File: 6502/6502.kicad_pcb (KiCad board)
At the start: 2 copper layers, 188.3 x 191.4 mm, 52 parts, among them J1 Conn_01x08, J10 Conn_02x20_Odd_Even, J11 Mini-DIN-6, J12 Conn_02x20_Odd_Even, J13 Jack-DC, J14 Conn_01x02, J2 Conn_01x08, J3 Conn_01x03, J4 Conn_02x20_Odd_Even, J5 Conn_01x08, J6 Conn_01x05, J7 Conn_02x20_Odd_Even, J8 Conn_01x02, J9 Conn_01x02, Q1 FQP47P06, SW1 SW_Push, SW2 SW_Push, U1 74LS08, U10 LM7805_TO220, U2 74LS154, U3 28C256, U4 ATF22V10C, U5 65C02S, U6 AS6C4008-55PCN, U7 6522, U8 6522, U9 NHD-0420H1Z, X1 ACO-4MHz

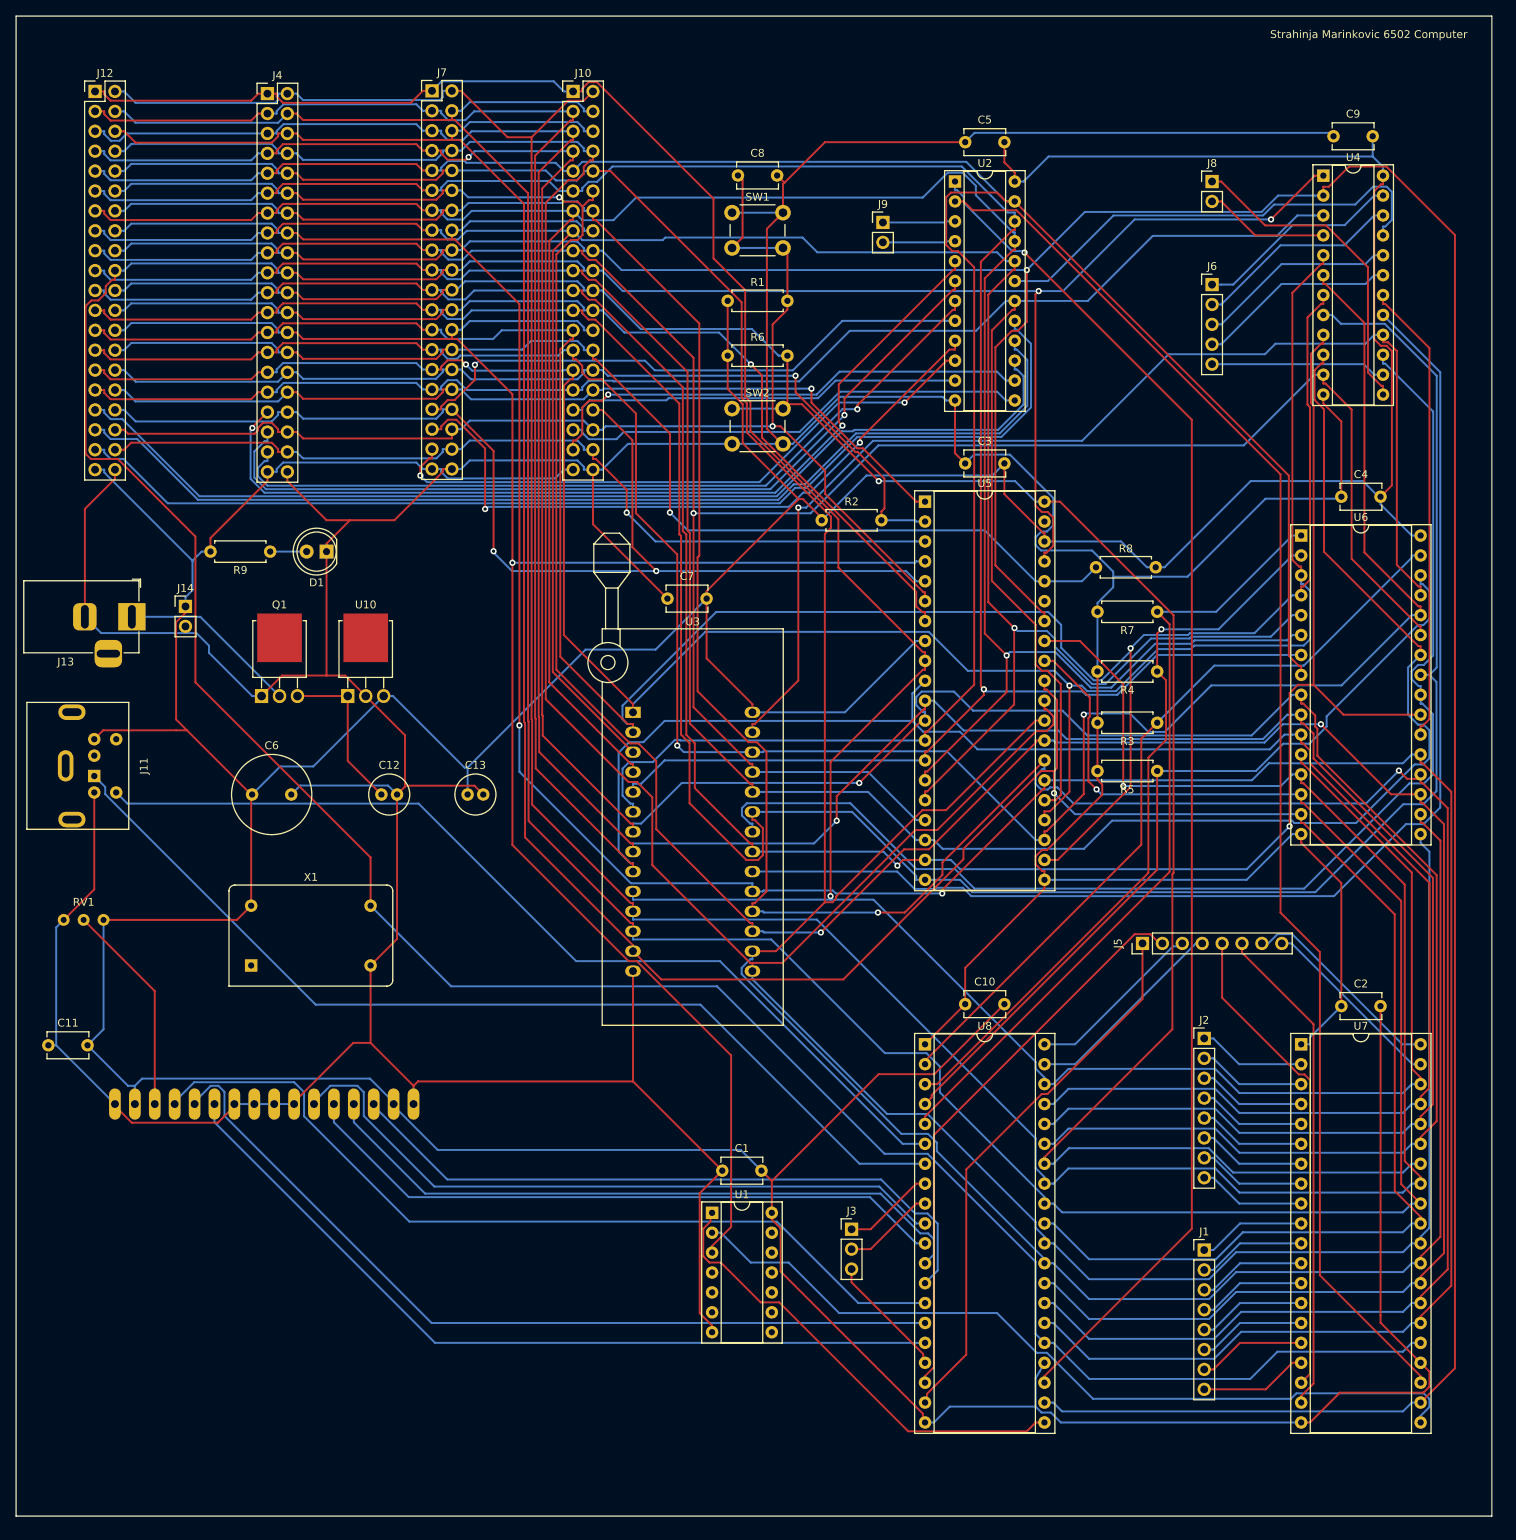
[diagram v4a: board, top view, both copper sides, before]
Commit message: added mount holes
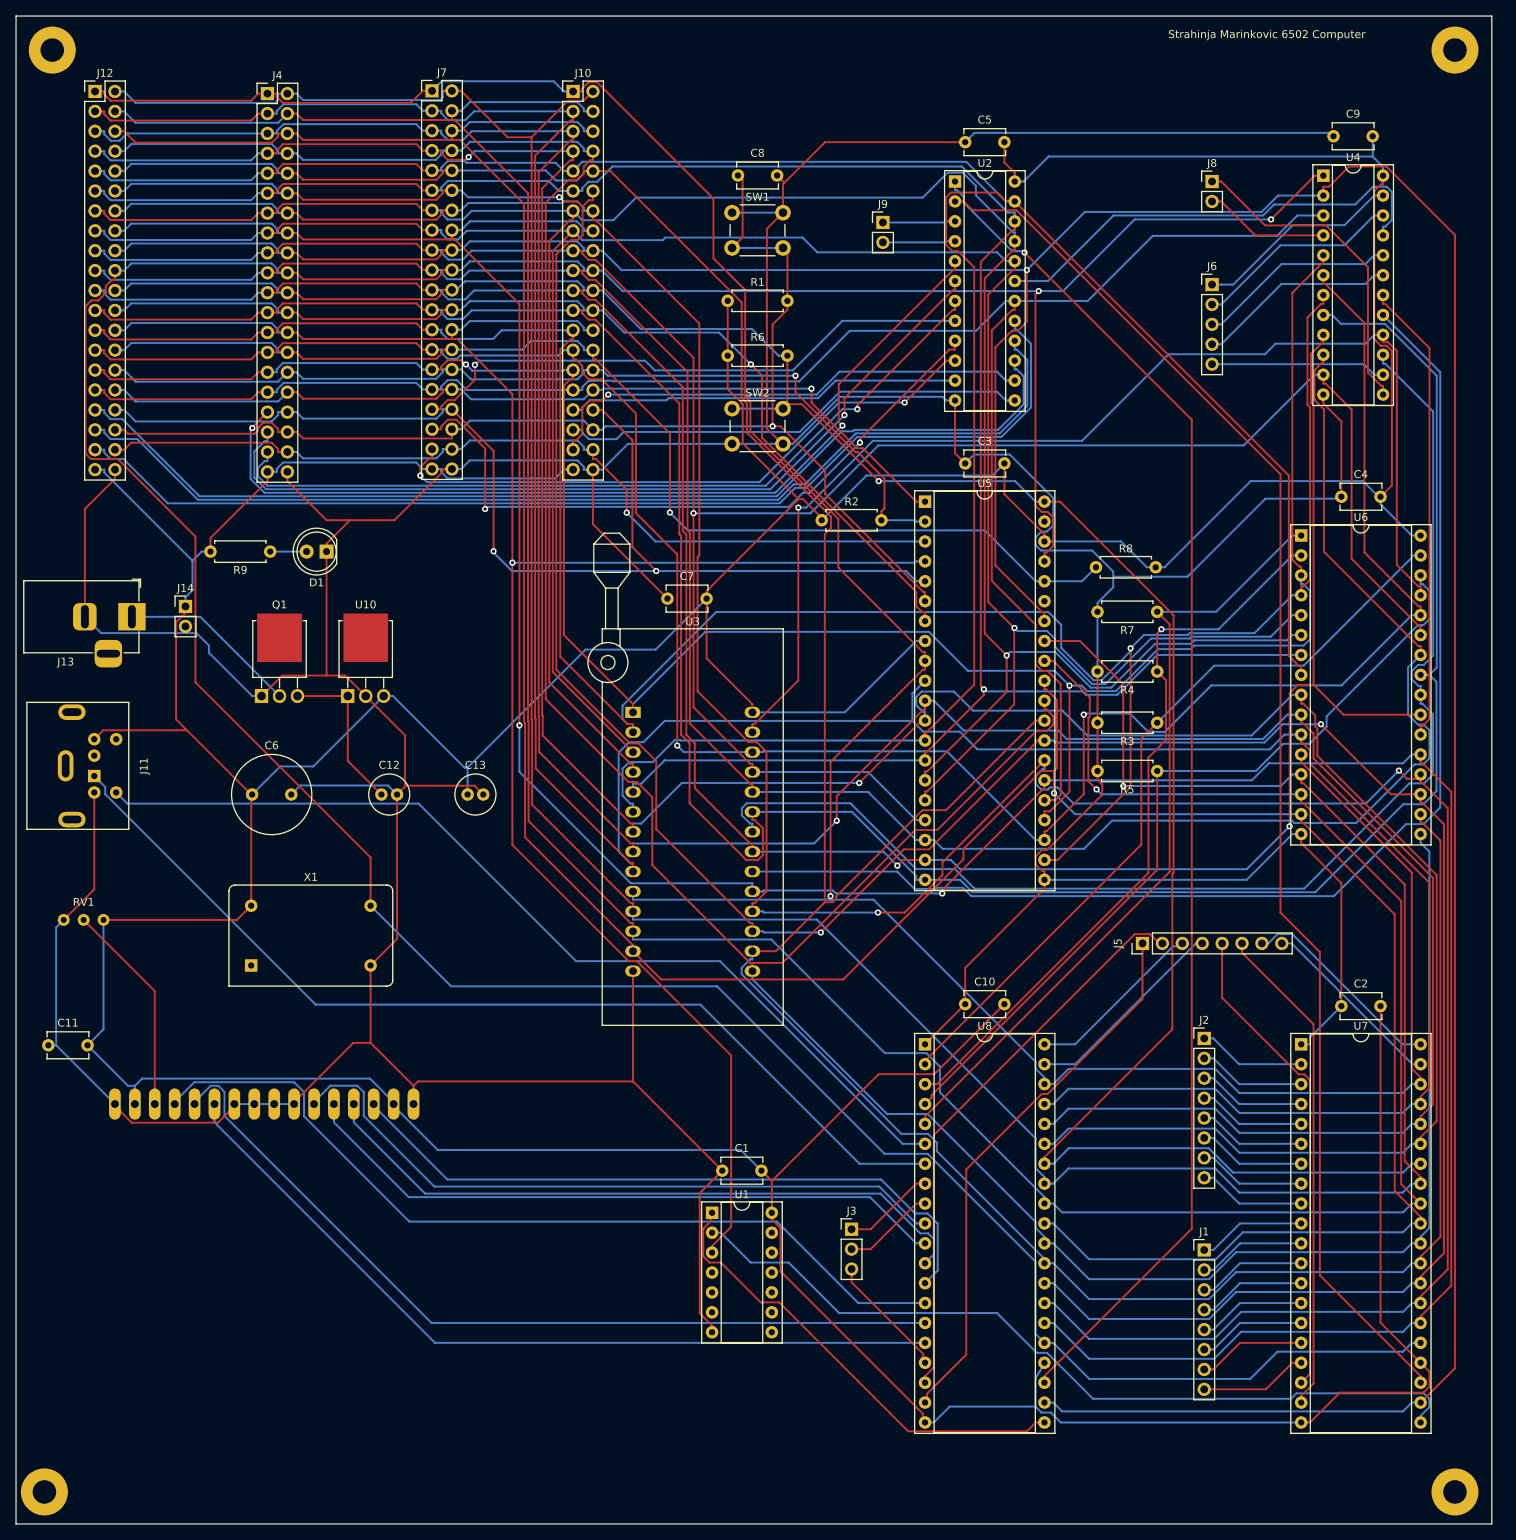
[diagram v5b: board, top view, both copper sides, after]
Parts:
- added REF**: MountingHole_3mm_Pad, MountingHole:MountingHole_3mm_Pad, F.Cu at (312.0, 259.0)
- added REF**: MountingHole_3mm_Pad, MountingHole:MountingHole_3mm_Pad, F.Cu at (133.0, 75.0)
- added REF**: MountingHole_3mm_Pad, MountingHole:MountingHole_3mm_Pad, F.Cu at (132.0, 259.0)
- added REF**: MountingHole_3mm_Pad, MountingHole:MountingHole_3mm_Pad, F.Cu at (312.0, 75.0)
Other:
- board size 188.3 x 191.4 mm -> 188.3 x 192.4 mm
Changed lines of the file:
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@@
     )
+  )
+  (footprint "MountingHole:MountingHole_3mm_Pad" (layer "F.Cu")
+    (at 312 259)
+    (descr "Mounting Hole 3mm")
+    (tags "mounting hole 3mm")
+    (attr exclude_from_pos_files exclude_from_bom)
+    (fp_text reference "REF**" (at 0 -5) (layer "F.SilkS") hide
+      (effects (font (size 1 1) (thickness 0.15)))
+    )
+    (fp_text value "MountingHole_3mm_Pad" (at 0 4) (layer "F.Fab")
+      (effects (font (size 1 1) (thickness 0.15)))
+    )
+    (fp_text user "${REFERENCE}" (at 0 0) (layer "F.Fab")
+      (effects (font (size 1 1) (thickness 0.15)))
+    )
+    (fp_circle (center 0 0) (end 3 0) (layer "Cmts.User") (width 0.15) (fill none))
+    (fp_circle (center 0 0) (end 3.25 0) (layer "F.CrtYd") (width 0.05) (fill none))
+    (pad "1" thru_hole circle (at 0 0) (size 6 6) (drill 3) (layers *.Cu *.Mask))
   )
   (footprint "Connector_PinHeader_2.54mm:PinHeader_2x20_P2.54mm_Vertical" (layer "F.Cu")
@@
       (rotate (xyz 0 0 0))
     )
+  )
+  (footprint "MountingHole:MountingHole_3mm_Pad" (layer "F.Cu")
+    (at 133 75)
+    (descr "Mounting Hole 3mm")
+    (tags "mounting hole 3mm")
+    (attr exclude_from_pos_files exclude_from_bom)
+    (fp_text reference "REF**" (at 0 -4) (layer "F.SilkS") hide
+      (effects (font (size 1 1) (thickness 0.15)))
+    )
+    (fp_text value "MountingHole_3mm_Pad" (at 0 4) (layer "F.Fab")
+      (effects (font (size 1 1) (thickness 0.15)))
+    )
+    (fp_text user "${REFERENCE}" (at 0 0) (layer "F.Fab")
+      (effects (font (size 1 1) (thickness 0.15)))
+    )
+    (fp_circle (center 0 0) (end 3 0) (layer "Cmts.User") (width 0.15) (fill none))
+    (fp_circle (center 0 0) (end 3.25 0) (layer "F.CrtYd") (width 0.05) (fill none))
+    (pad "1" thru_hole circle (at 0 0) (size 6 6) (drill 3) (layers *.Cu *.Mask))
   )
   (footprint "LED_THT:LED_D5.0mm_Clear" (layer "F.Cu")
@@
     )
   )
+  (footprint "MountingHole:MountingHole_3mm_Pad" (layer "F.Cu")
+    (at 132 259)
+    (descr "Mounting Hole 3mm")
+    (tags "mounting hole 3mm")
+    (attr exclude_from_pos_files exclude_from_bom)
+    (fp_text reference "REF**" (at 0 -4) (layer "F.SilkS") hide
+      (effects (font (size 1 1) (thickness 0.15)))
+    )
+    (fp_text value "MountingHole_3mm_Pad" (at 0 4) (layer "F.Fab")
+      (effects (font (size 1 1) (thickness 0.15)))
+    )
+    (fp_text user "${REFERENCE}" (at 0 0) (layer "F.Fab")
+      (effects (font (size 1 1) (thickness 0.15)))
+    )
+    (fp_circle (center 0 0) (end 3 0) (layer "Cmts.User") (width 0.15) (fill none))
+    (fp_circle (center 0 0) (end 3.25 0) (layer "F.CrtYd") (width 0.05) (fill none))
+    (pad "1" thru_hole circle (at 0 0) (size 6 6) (drill 3) (layers *.Cu *.Mask))
+  )
   (footprint "Resistor_THT:R_Axial_DIN0207_L6.3mm_D2.5mm_P7.62mm_Horizontal" (layer "F.Cu")
     (at 219.19 107)
@@
     )
   )
+  (footprint "MountingHole:MountingHole_3mm_Pad" (layer "F.Cu")
+    (at 312 75)
+    (descr "Mounting Hole 3mm")
+    (tags "mounting hole 3mm")
+    (attr exclude_from_pos_files exclude_from_bom)
+    (fp_text reference "REF**" (at 0 -4) (layer "F.SilkS") hide
+      (effects (font (size 1 1) (thickness 0.15)))
+    )
+    (fp_text value "MountingHole_3mm_Pad" (at 0 4) (layer "F.Fab")
+      (effects (font (size 1 1) (thickness 0.15)))
+    )
+    (fp_text user "${REFERENCE}" (at 0 0) (layer "F.Fab")
+      (effects (font (size 1 1) (thickness 0.15)))
+    )
+    (fp_circle (center 0 0) (end 3 0) (layer "Cmts.User") (width 0.15) (fill none))
+    (fp_circle (center 0 0) (end 3.25 0) (layer "F.CrtYd") (width 0.05) (fill none))
+    (pad "1" thru_hole circle (at 0 0) (size 6 6) (drill 3) (layers *.Cu *.Mask))
+  )
   (footprint "Capacitor_THT:C_Disc_D5.1mm_W3.2mm_P5.00mm" (layer "F.Cu")
     (at 132.5 202)
@@
     )
   )
-  (gr_rect (start 128.38 262.08) (end 316.7 70.66) (layer "Edge.Cuts") (width 0.1) (fill none))
-  (gr_text "Strahinja Marinkovic 6502 Computer" (at 301 73) (layer "F.SilkS")
+  (gr_rect (start 128.38 263.08) (end 316.7 70.66) (layer "Edge.Cuts") (width 0.1) (fill none))
+  (gr_text "Strahinja Marinkovic 6502 Computer" (at 288 73) (layer "F.SilkS")
     (effects (font (size 1 1) (thickness 0.15)))
   )
+  (target plus (at 131 259) (size 5) (width 0.1) (layer "Edge.Cuts"))
+  (target plus (at 132 259) (size 5) (width 0.1) (layer "Edge.Cuts"))
   (segment (start 231.19 135) (end 231.19 134.6921) (width 0.25) (layer "F.Cu") (net 1))
   (segment (start 302.5 236.4709) (end 302.5 197) (width 0.25) (layer "F.Cu") (net 1))
